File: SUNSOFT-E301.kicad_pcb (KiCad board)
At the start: 2 copper layers, 91.3 x 58.3 mm, 27 parts, among them J1 Famicom Card Edge Connector, U1 HM6264, U2 FME7-5A-5B, U3 27C040, U4 27C020

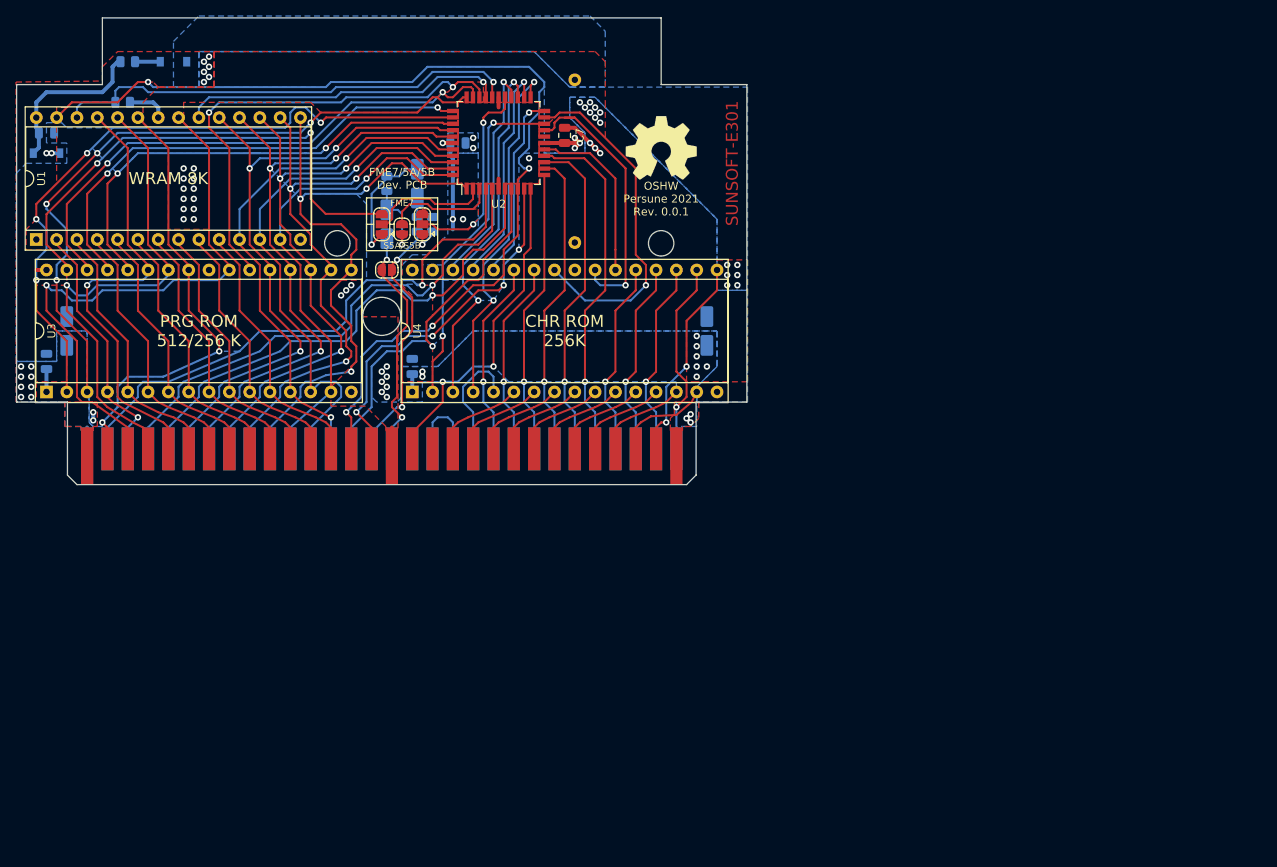
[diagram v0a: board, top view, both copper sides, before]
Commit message: Revision 0.0.2
- connect CIRAM A10
- improve plane distribution
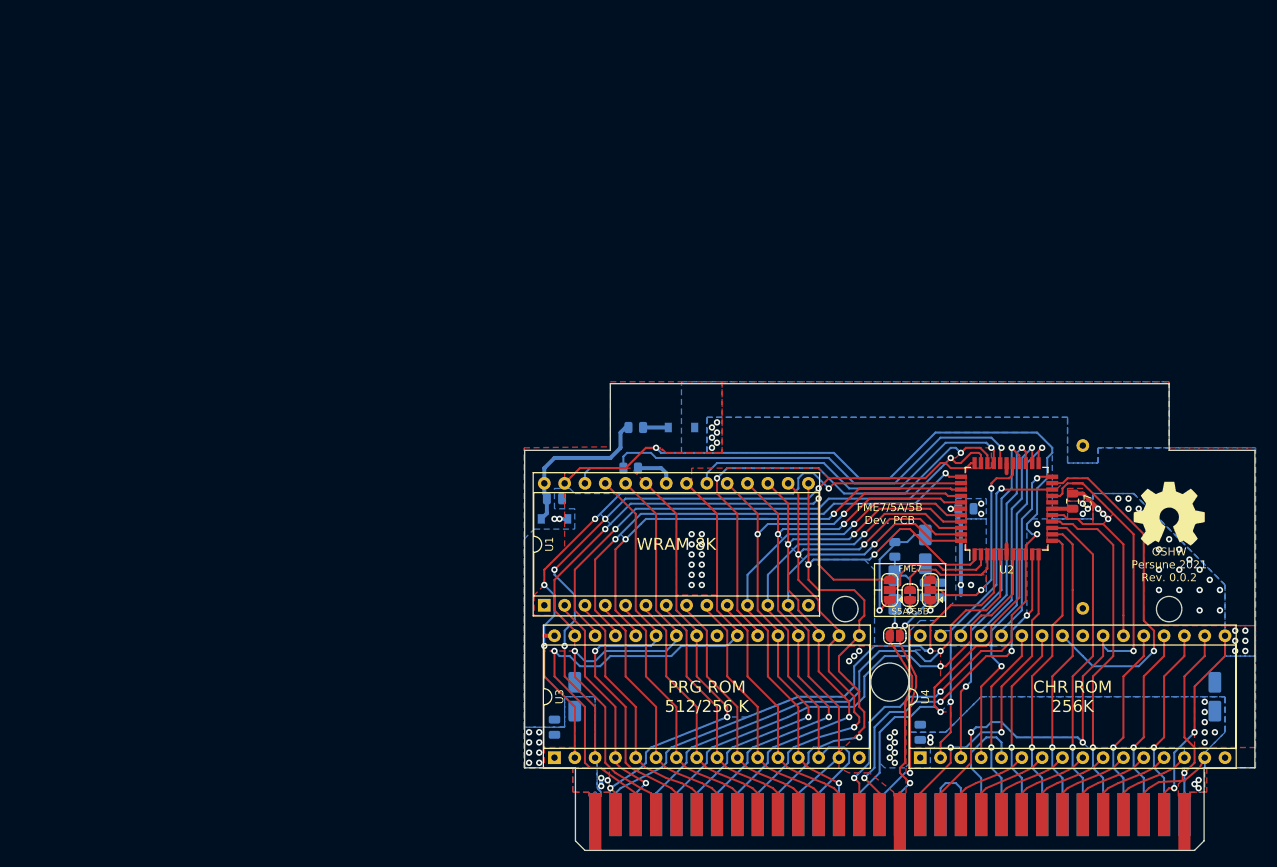
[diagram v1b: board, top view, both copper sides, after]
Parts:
- J1: footprint card-edge-connectors:GRM-E301 -> custom footprints:GRM-E301
- moved C6 78.2 mm to (161.9, 87.0)
- moved BT1 78.2 mm to (176.5, 87.0)
- moved C1 78.2 mm to (110.5, 85.7)
- moved C2 78.2 mm to (156.8, 92.1)
- moved C3 78.2 mm to (153.0, 97.2)
- moved C4 78.2 mm to (110.5, 114.3)
- moved C5 78.2 mm to (156.2, 114.9)
- moved C8 78.2 mm to (193.0, 110.5)
- moved C9 78.2 mm to (113.0, 110.5)
- moved D1 78.2 mm to (110.5, 88.3)
- moved D2 78.2 mm to (126.4, 76.8)
- moved J1 78.2 mm to (152.4, 119.4)
- moved JP1 78.2 mm to (152.4, 97.2)
- moved JP2 78.2 mm to (154.9, 97.8)
- moved JP4 78.2 mm to (153.0, 102.9)
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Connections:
- J1 pad 18: Net-(J1-Pad18) -> /CHR_A10
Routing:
- net /CHR_A10: track 35.0 -> 76.9 mm, vias 1 -> 3
- net VCC: track 38.5 -> 26.5 mm
- net /WRAM_~CE: track 40.7 -> 43.3 mm
- net /PRG_~CE: track 59.1 -> 61.7 mm
- net /CPU_R~W: track 128.3 -> 130.9 mm
- net /WRAM_CE: track 59.1 -> 61.7 mm
- net /CPU_D3: track 79.8 -> 81.7 mm
- net /CHR_A15: track 45.6 -> 44.0 mm
- net /PPU_A10: track 35.8 -> 37.4 mm
- net /CPU_A11: track 56.1 -> 54.9 mm
- net /M2: track 69.0 -> 67.9 mm
- net /AUD_IN: track 32.0 -> 31.0 mm
- net /AUD_OUT: track 29.7 -> 28.9 mm
- net /PPU_A12: track 41.3 -> 40.6 mm
- net GND: vias 38 -> 53
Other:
- outline, holes or cut-outs redrawn
- board text added: "OSHW Persune 2021 Rev. 0.0.2"
- board text removed: "OSHW Persune 2021 Rev. 0.0.1"

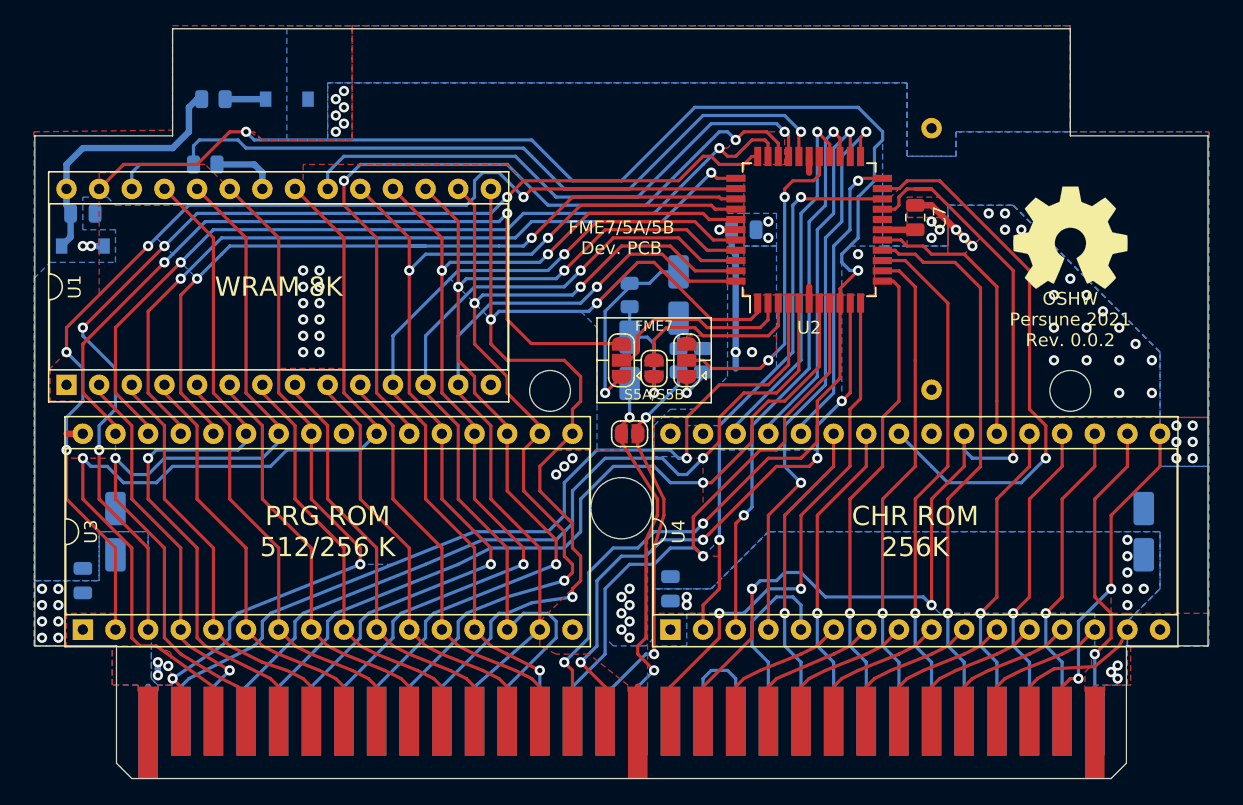
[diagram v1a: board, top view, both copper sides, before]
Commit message: Revision 0.0.3
- updated outline to match Barcode World
- added pixel sprite art by @yoeynsf
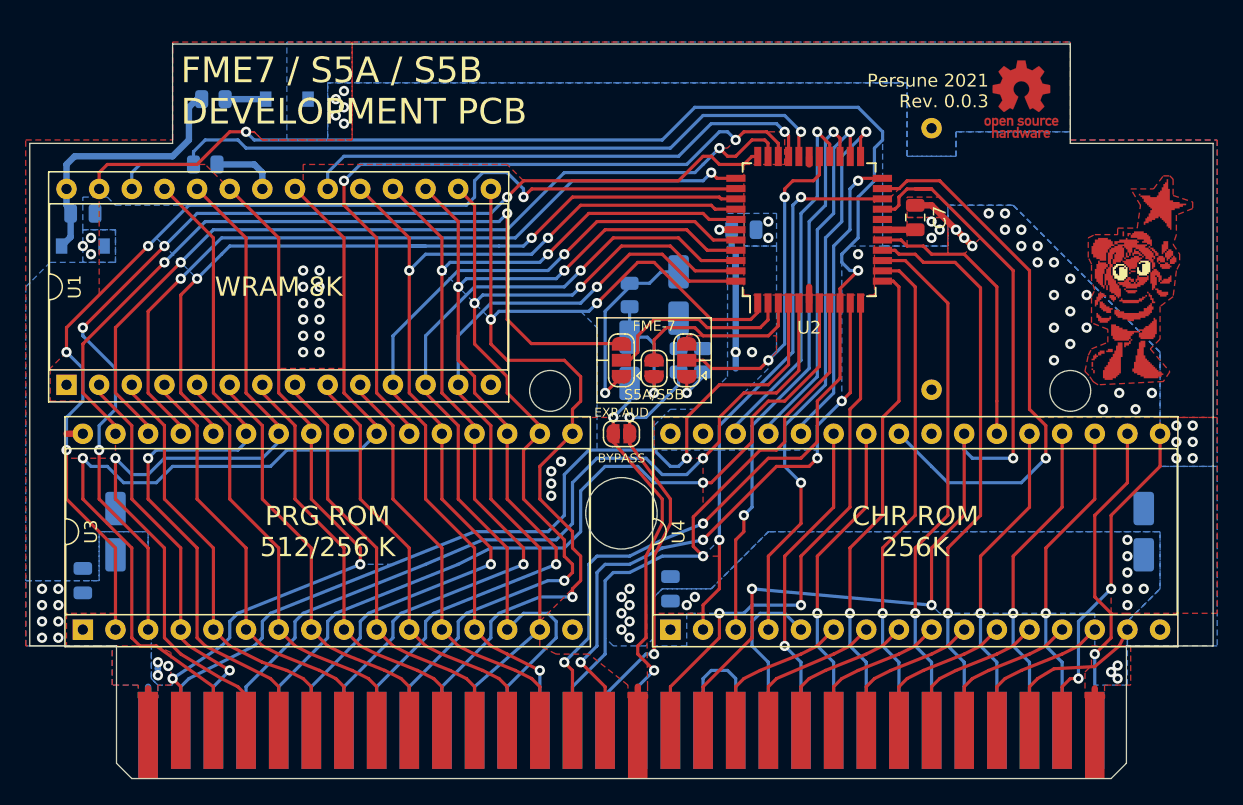
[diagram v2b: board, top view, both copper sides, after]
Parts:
- removed the REF** at (187.3, 87.6)
- added REF**: OSHW-Logo_5.7x6mm_Copper, Symbol:OSHW-Logo_5.7x6mm_Copper, F.Cu at (183.5, 76.8)
- J1: footprint custom footprints:GRM-E301 -> custom footprints:BBW-E301
- moved JP1 0.63 mm to (152.4, 102.9)
- renumbered JP4 to JP1, JP1 to JP2, JP2 to JP3, JP3 to JP4
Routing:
- net /WRAM_CE: track 61.7 -> 58.8 mm
- net /WRAM_~CE: track 43.3 -> 40.7 mm
- net /PRG_~CE: track 61.7 -> 59.1 mm
- net /PPU_A7: track 15.1 -> 12.9 mm
- net VCC: track 26.5 -> 24.5 mm
- net /CPU_R~W: track 130.9 -> 128.9 mm
- net /AUD_IN: track 31.0 -> 32.8 mm
- net /CHR_A10: track 76.9 -> 75.3 mm
- net /AUD_OUT: track 28.9 -> 29.8 mm
- net /M2: track 67.9 -> 68.8 mm
- net /PPU_~RD: track 41.3 -> 42.0 mm
- net GND: track 21.4 -> 20.7 mm, vias 53 -> 52
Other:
- board size 91.3 x 58.3 mm -> 92.1 x 57.1 mm
- net class Default: clearance 0.2 -> 0.01
- net class Power: clearance 0.2 -> 0.01
- rule trace_clearance: 0.2 -> 0.01
- board text added: "BYPASS"
- board text added: "EXP.AUD"
- board text added: "FME-7"
- board text added: "FME7 / S5A / S5B DEVELOPMENT PCB"
- board text added: "Persune 2021 Rev. 0.0.3"
- board text added: "SS-E301"
- board text removed: "FME7"
- board text removed: "FME7/5A/5B Dev. PCB"
- board text removed: "OSHW Persune 2021 Rev. 0.0.2"
- board text removed: "SUNSOFT-E301"

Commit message: KiCad 6.0
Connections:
- net /CHR_~CE renamed /CHR_~{CE}
- net /CPU_R~W renamed /CPU_R~{W}
- net /PPU_~RD renamed /PPU_~{RD}
- net /PRG_~CE renamed /PRG_~{CE}
- net /WRAM_~CE renamed /WRAM_~{CE}
- net /~IRQ renamed /~{IRQ}
- net /~ROMSEL renamed /~{ROMSEL}
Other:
- net class Default removed
- net class Power removed
